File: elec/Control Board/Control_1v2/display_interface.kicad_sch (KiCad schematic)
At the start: 20 parts, among them J35 Conn_02x05_Odd_Even, J36 Conn_02x05_Odd_Even, J801 Conn_01x03_0.1", J802 Con_01x02_0.1", J803 Screw_Terminal_01x04_5.08mm, J804 Screw_Terminal_01x02_5.08mm, J805 Con_01x02_0.1", K801 Relay SRU-12VDC, Q601 BSS138

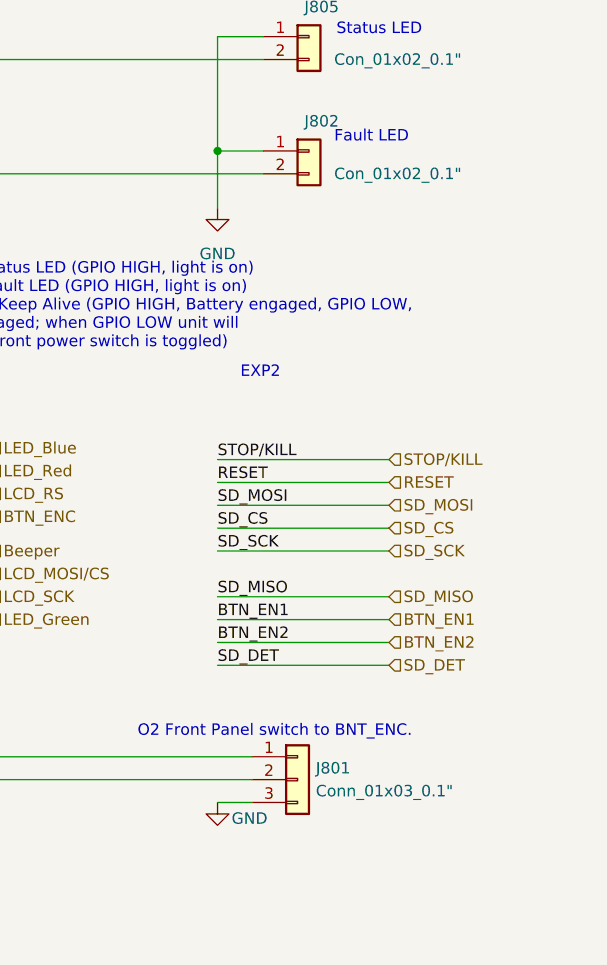
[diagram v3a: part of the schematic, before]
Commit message: PCB V1.2. Fixes to parts for BOM and PL.
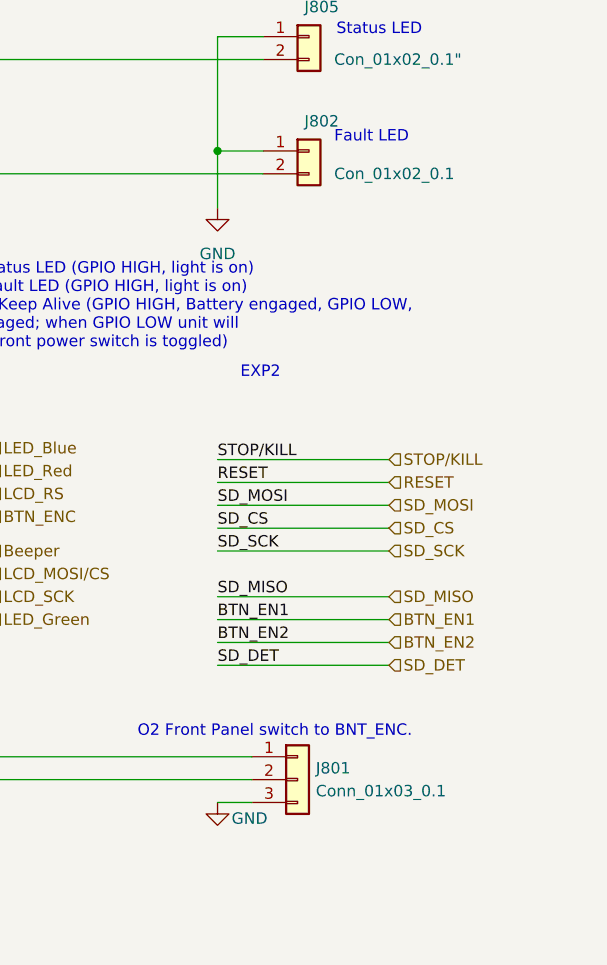
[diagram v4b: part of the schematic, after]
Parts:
- J801: value Conn_01x03_0.1" -> Conn_01x03_0.1
- J802: value Con_01x02_0.1" -> Con_01x02_0.1
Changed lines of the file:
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@@
       (effects (font (size 1.27 1.27)) (justify left))
     )
-    (property "Value" "Con_01x02_0.1\"" (at 261.874 91.44 0)
+    (property "Value" "Con_01x02_0.1" (at 261.874 91.44 0)
       (effects (font (size 1.27 1.27)) (justify left))
     )
@@
       (effects (font (size 1.27 1.27)) (justify left))
     )
-    (property "Value" "Conn_01x03_0.1\"" (at 259.842 160.02 0)
-      (effects (font (size 1.27 1.27)) (justify left))
-    )
+    (property "Value" "Conn_01x03_0.1" (at 259.842 160.02 0)
+      (effects (font (size 1.27 1.27)) (justify left))
+    )

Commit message: Control_1v2.kicad_pcb and schematic, Change J804 to JILN JL500-50802G01 screw terminal. Fix Incompatible part called out for J804, C5142622. #374
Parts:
- J804: Distributor 1 PN C5142622 -> C709041; MPN GS010B-5.08-2*02P-11-1000A(H) -> JL500-50802G01; Manufacturer GOOSVN -> JILN
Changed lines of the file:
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@@
       (effects (font (size 1.27 1.27)) hide)
     )
-    (property "Datasheet" "~" (at 259.08 55.88 0)
+    (property "Datasheet" "https://www.lcsc.com/datasheet/lcsc_datasheet_2411011430_JILN-JL500-50802G01_C709041.pdf" (at 259.08 55.88 0)
       (effects (font (size 1.27 1.27)) hide)
     )
@@
       (effects (font (size 1.27 1.27)) hide)
     )
-    (property "Description" "Screw_Terminal_01x02_5.08mm " (at 259.08 55.88 0)
+    (property "Description" "Screw _Terminal_01x02_5.08mm 15A 300V Green 14~26 AWG" (at 259.08 55.88 0)
       (effects (font (size 1.27 1.27)) hide)
     )
@@
       (effects (font (size 1.27 1.27)) hide)
     )
-    (property "Distributor 1 PN" "C5142622" (at 259.08 55.88 0)
+    (property "Distributor 1 PN" "C709041" (at 259.08 55.88 0)
       (effects (font (size 1.27 1.27)) hide)
     )
-    (property "MPN" "GS010B-5.08-2*02P-11-1000A(H)" (at 259.08 55.88 0)
+    (property "MPN" "JL500-50802G01" (at 259.08 55.88 0)
       (effects (font (size 1.27 1.27)) hide)
     )
-    (property "Manufacturer" "GOOSVN" (at 259.08 55.88 0)
+    (property "Manufacturer" "JILN" (at 259.08 55.88 0)
       (effects (font (size 1.27 1.27)) hide)
     )
